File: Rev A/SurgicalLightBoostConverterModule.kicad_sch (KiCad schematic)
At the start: 0 parts

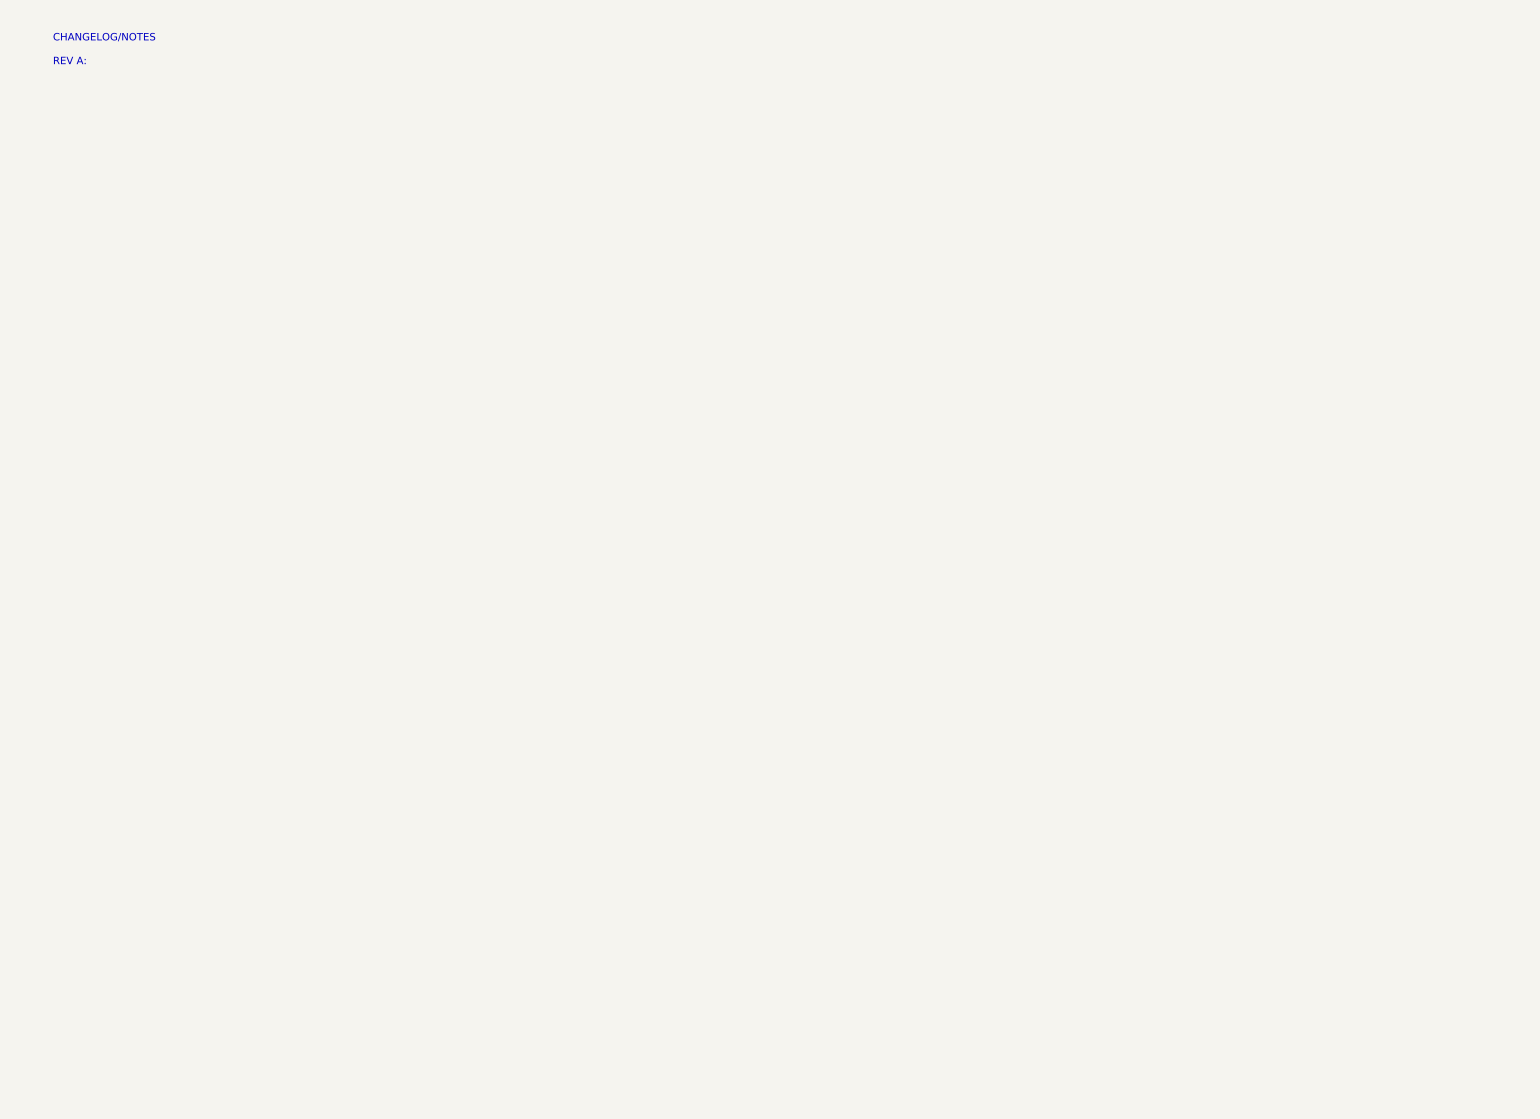
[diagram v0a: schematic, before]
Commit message: Added boost converter.
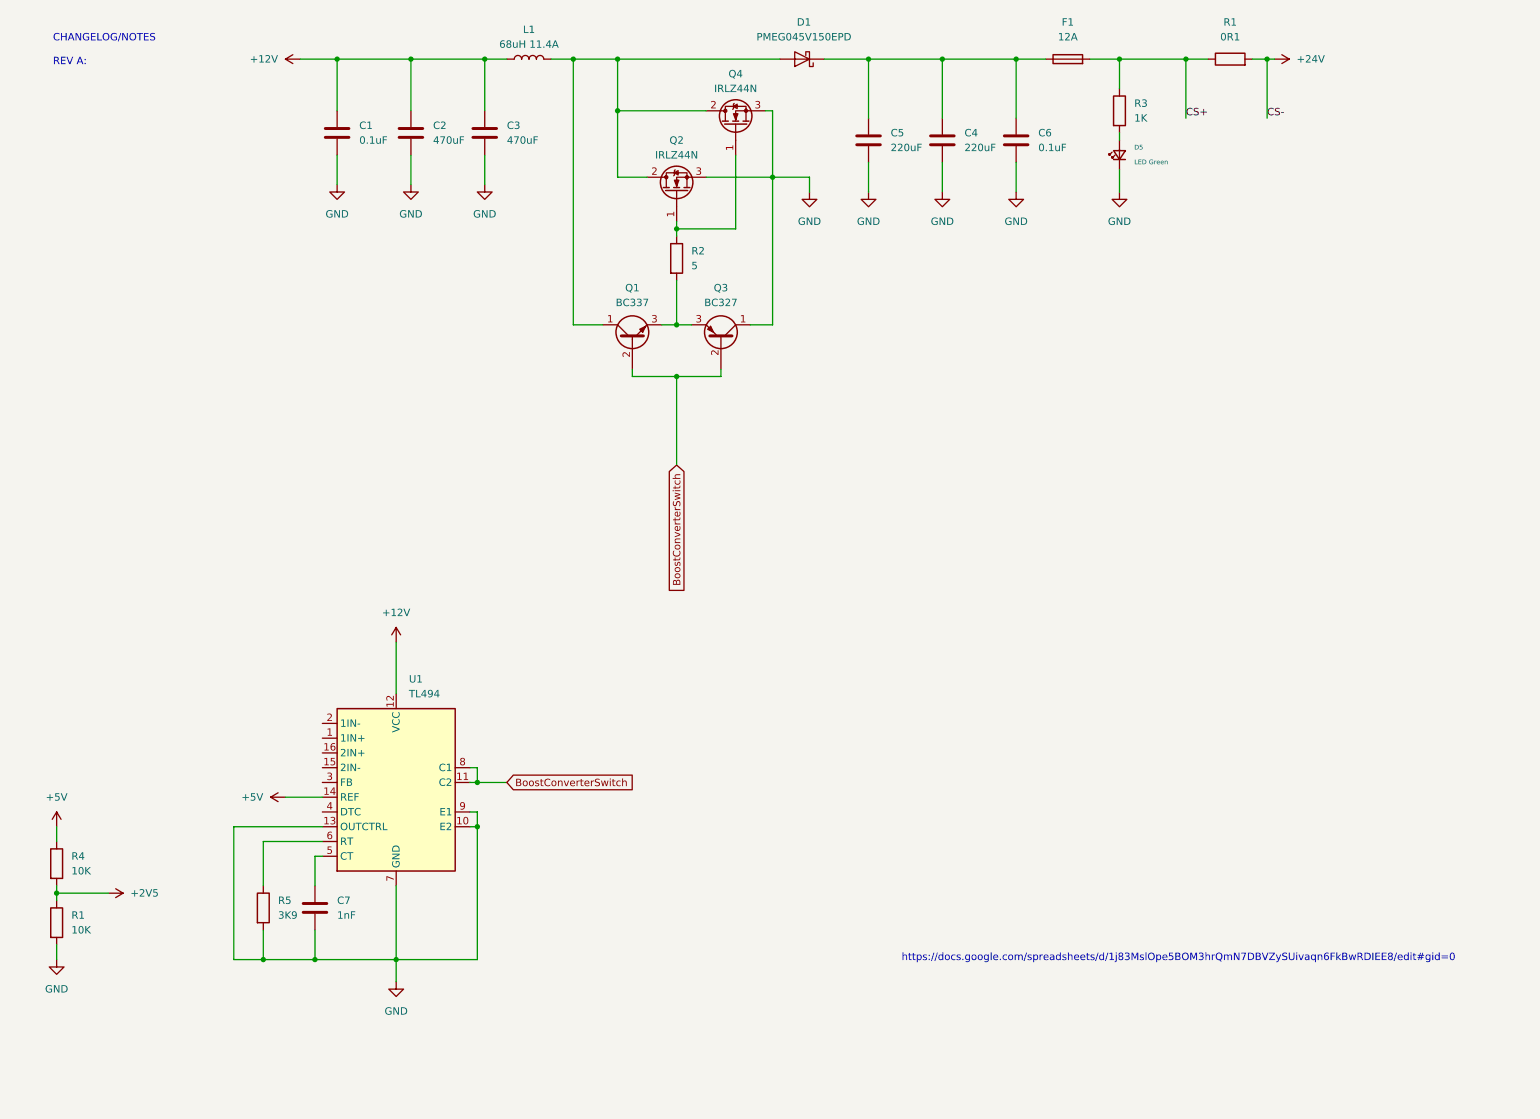
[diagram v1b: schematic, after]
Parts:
- added C1, C6: 0.1uF, Capacitor_SMD:C_0805_2012Metric, symbol Device:C
- added C2, C3: 470uF, symbol Device:C
- added C4, C5: 220uF, symbol Device:C
- added C7: 1nF, Capacitor_SMD:C_0805_2012Metric, symbol Device:C
- added D1: PMEG045V150EPD, Package_TO_SOT_SMD:Nexperia_CFP15_SOT-1289, symbol Diode:PMEG045V150EPD
- added D5: LED Green, LED_SMD:LED_0805_2012Metric, symbol Device:LED_Small
- added F1: 12A, symbol Device:Fuse
- added L1: 68uH 11.4A, symbol Device:L
- added Q1: BC337, Package_TO_SOT_THT:TO-92_Inline, symbol Transistor_BJT:BC337
- added Q2, Q4: IRLZ44N, Package_TO_SOT_THT:TO-220-3_Vertical, symbol Transistor_FET:IRLZ44N
- added Q3: BC327, Package_TO_SOT_THT:TO-92_Inline, symbol Transistor_BJT:BC327
- added R1: 0R1, Resistor_SMD:R_0805_2012Metric, symbol Device:R
- added R1, R4: 10K, Resistor_SMD:R_0805_2012Metric, symbol Device:R
- added R2: 5, Resistor_SMD:R_0805_2012Metric, symbol Device:R
- added R3: 1K, Resistor_SMD:R_0805_2012Metric, symbol Device:R
- added R5: 3K9, Resistor_SMD:R_0805_2012Metric, symbol Device:R
- added U1: TL494, symbol Regulator_Controller:TL494
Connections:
- new net: D1.1 (A), D1.2 (A), L1.2, Q1.1 (C), Q2.2 (D), Q4.2 (D)
- new net: Q1.3 (E), Q3.3 (E), R2.2
- new net: C4.1, C5.1, C6.1, D1.3 (K), F1.1
- new net: R5.1, U1.6 (RT)
- new net: Q2.1 (G), Q4.1 (G), R2.1
- new net: C7.1, U1.5 (CT)
- new net: D5.2 (A), R3.2
- new net +12V: C1.1, C2.1, C3.1, L1.1, U1.12 (VCC)
- new net +24V: R1.2
- new net +2V5: R1.1, R4.2
- new net +5V: R4.1, U1.14 (REF)
- new net BoostConverterSwitch: Q1.2 (B), Q3.2 (B), U1.11 (C2), U1.8 (C1)
- new net CS+: F1.2, R1.1, R3.1
- new net GND: C1.2, C2.2, C3.2, C4.2, C5.2, C6.2, C7.2, D5.1 (K), Q2.3 (S), Q3.1 (C), Q4.3 (S), R1.2, R5.2, U1.10 (E2), U1.13 (OUTCTRL), U1.7 (GND), U1.9 (E1)
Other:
- note added: "https://docs.google.com/spreadsheets/d/1j83MslOpe5BOM3hrQmN7DBVZySUivaqn6FkBwRDIEE8/edit#gid=0"

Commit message: Added feedback and protection circuits.
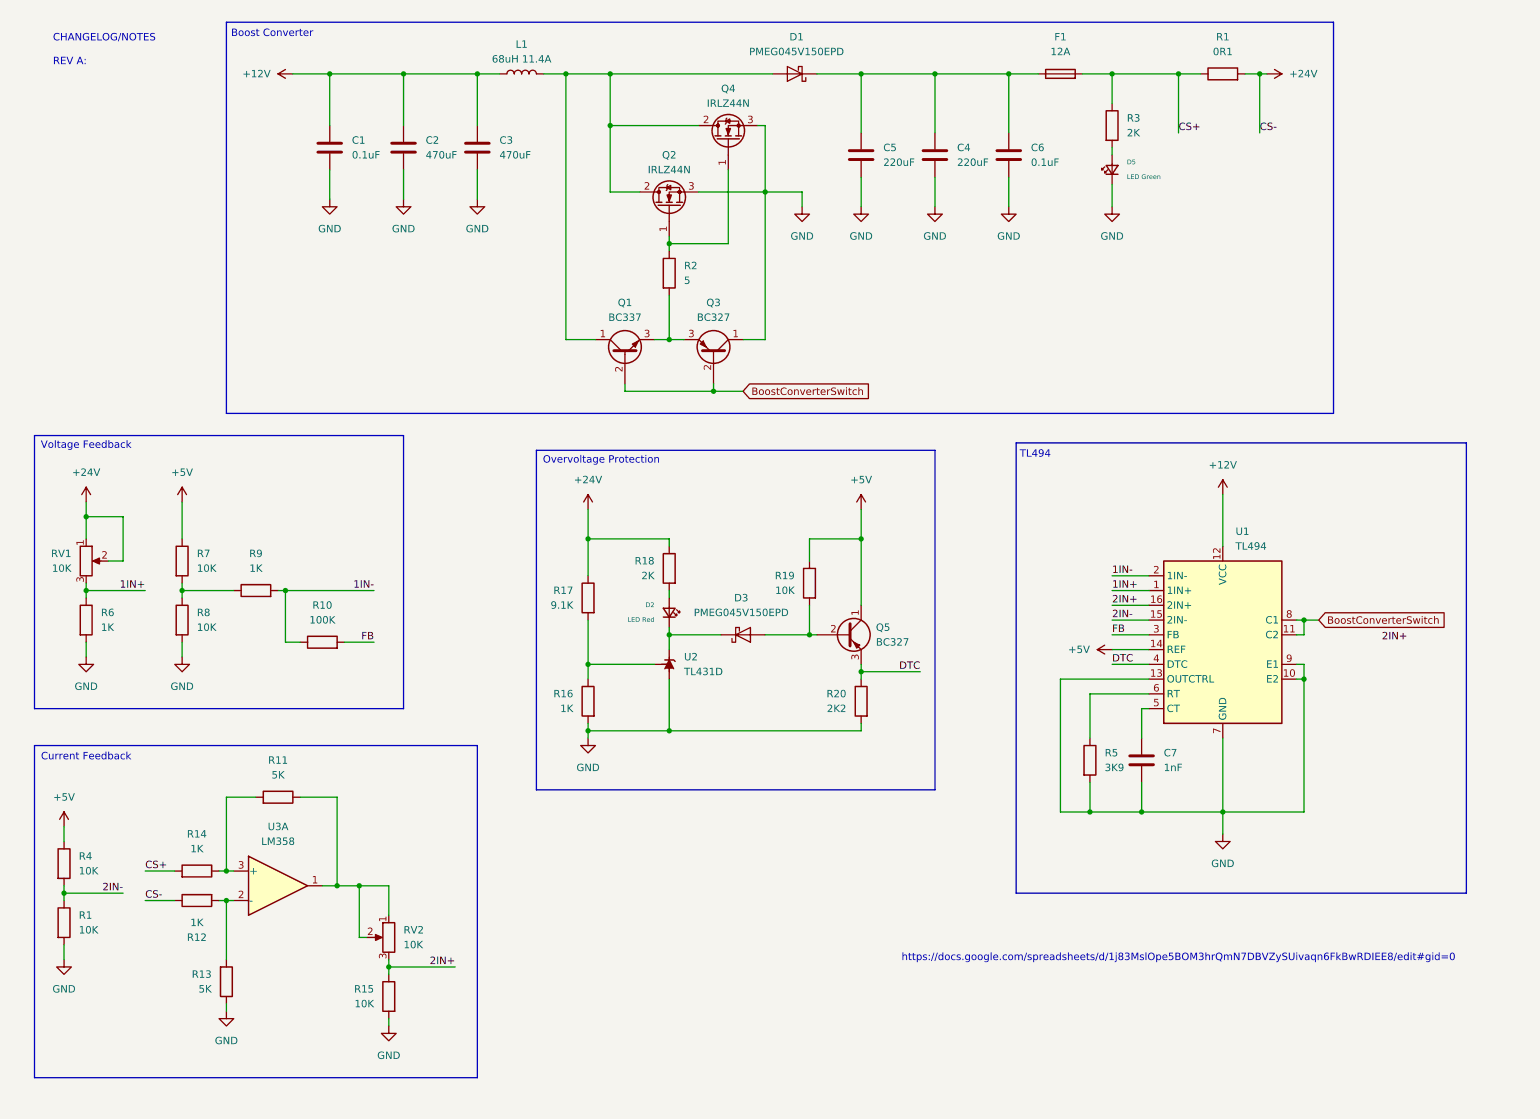
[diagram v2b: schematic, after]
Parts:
- added D2: LED Red, LED_SMD:LED_0805_2012Metric, symbol Device:LED_Small
- added D3: PMEG045V150EPD, Package_TO_SOT_SMD:Nexperia_CFP15_SOT-1289, symbol Diode:PMEG045V150EPD
- added Q5: BC327, Package_TO_SOT_THT:TO-92_Inline, symbol Transistor_BJT:BC327
- added R10: 100K, Resistor_SMD:R_0805_2012Metric, symbol Device:R
- added R11, R13: 5K, Resistor_SMD:R_0805_2012Metric, symbol Device:R
- added R12, R14, R16, R6, R9: 1K, Resistor_SMD:R_0805_2012Metric, symbol Device:R
- added R15, R19, R7, R8: 10K, Resistor_SMD:R_0805_2012Metric, symbol Device:R
- added R17: 9.1K, Resistor_SMD:R_0805_2012Metric, symbol Device:R
- added R18: 2K, Resistor_SMD:R_0805_2012Metric, symbol Device:R
- added R20: 2K2, Resistor_SMD:R_0805_2012Metric, symbol Device:R
- added RV1, RV2: 10K, symbol Device:R_Potentiometer
- added U2: TL431D, Package_SO:SOIC-8_3.9x4.9mm_P1.27mm, symbol Reference_Voltage:TL431D
- added U3: LM358, symbol Amplifier_Operational:LM358
- R3: value 1K -> 2K
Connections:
- net +2V5 is gone; now on net 2IN-: R1.1, R4.2
- net +24V: now also R12.1, R17.1, R18.1, RV1.1, RV1.2
- net +5V: now also Q5.1 (C), R19.1, R7.1
- net CS+: now also R14.2
- net GND: now also R13.1, R15.2, R16.2, R20.2, R6.2, R8.2, U2.2 (A), U2.3 (A), U2.6 (A), U2.7 (A)
- net 1IN+: now reaches U1.1 (1IN+)
- net 1IN+: now also R6.1, RV1.3
- net 2IN-: now reaches U1.15 (2IN-)
- net 2IN+: now reaches U1.16 (2IN+)
- net 2IN+: now also R15.1, RV2.3
- net 1IN-: now reaches U1.2 (1IN-)
- net 1IN-: now also R10.1, R9.2
- net FB: now reaches U1.3 (FB)
- net FB: now also R10.2
- net DTC: now reaches U1.4 (DTC)
- net DTC: now also Q5.3 (E), R20.1
- new net: R11.2, R14.1, U3.3 (+)
- new net: R11.1, RV2.1, RV2.2, U3.1
- new net: R12.2, R13.2, U3.2 (-)
- new net: R16.1, R17.2, U2.8 (REF)
- new net: D3.1 (A), D3.2 (A), Q5.2 (B), R19.2
- new net: D2.2 (A), R18.2
- new net: D2.1 (K), D3.3 (K), U2.1 (K)
- new net: R7.2, R8.1, R9.1
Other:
- note added: "Boost Converter"
- note added: "Current Feedback"
- note added: "Overvoltage Protection"
- note added: "TL494"
- note added: "Voltage Feedback"
- moved on the sheet: C1, C2, C3, C4, C5, C6, C7, D1, D5, F1, L1, Q1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

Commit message: More schematic updates.
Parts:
- added D4: LED Green, LED_SMD:LED_0805_2012Metric, symbol Device:LED_Small
- added H1, H2, H3, H4: M3 Hole, MountingHole:MountingHole_3.2mm_M3_Pad_TopBottom, symbol Mechanical:MountingHole_Pad
- added R21: 1K, Resistor_SMD:R_0805_2012Metric, symbol Device:R
- added TP1: 24V, symbol Connector:TestPoint_Small
- added TP2: 5V, symbol Connector:TestPoint_Small
- added TP3: DTC, symbol Connector:TestPoint_Small
- added TP4: PWM, symbol Connector:TestPoint_Small
- added TP5: 2IN+, symbol Connector:TestPoint_Small
- added TP6: 2IN-, symbol Connector:TestPoint_Small
- added TP7: 1IN+, symbol Connector:TestPoint_Small
- added TP8: 1IN-, symbol Connector:TestPoint_Small
- C2, C3: footprint (none) -> Capacitor_THT:CP_Radial_D12.5mm_P5.00mm
- C4, C5: footprint (none) -> Capacitor_THT:CP_Radial_D10.0mm_P5.00mm
- L1: footprint (none) -> Inductor_THT:L_Radial_D29.8mm_P29.30mm_Murata_1400series
- RV1, RV2: footprint (none) -> Connector_PinHeader_2.54mm:PinHeader_1x03_P2.54mm_Vertical
- U1: footprint (none) -> Package_DIP:DIP-16_W7.62mm
- U3: footprint (none) -> Package_DIP:DIP-8_W7.62mm_Socket
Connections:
- net +12V: now also H4.1, R21.1
- net +24V: now also H3.1, TP1.1
- net +5V: now also TP2.1
- net 1IN+: now also TP7.1
- net 1IN-: now also TP8.1
- net 2IN+: now also TP5.1
- net 2IN-: now also TP6.1
- net BoostConverterSwitch: now also TP4.1
- net DTC: now also TP3.1
- net GND: now also D4.1 (K), H1.1, H2.1
- new net: D4.2 (A), R21.2
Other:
- note added: "Mounting Holes for Power Connections"
- moved on the sheet: C1, C2, C4, C5, C6, C7, D1, D2, D3, D5, F1, L1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

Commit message: PCB? :(
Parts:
- added C10, C7: 1uF, Capacitor_SMD:C_0805_2012Metric, symbol Device:C
- added C11, C8: 0.1uF, Capacitor_SMD:C_0805_2012Metric, symbol Device:C
- added D4: LED Green, LED_SMD:LED_0805_2012Metric, symbol Device:LED_Small
- added R2: 0R1, Resistor_SMD:R_2512_6332Metric, symbol Device:R
- added R6: 330, Resistor_SMD:R_0805_2012Metric, symbol Device:R
- added unit 2 of U3
- added unit 3 of U3
- F1: footprint (none) -> Fuse:Fuse_1206_3216Metric_Pad1.42x1.75mm_HandSolder
- R1: footprint Resistor_SMD:R_0805_2012Metric -> Resistor_SMD:R_2512_6332Metric
- R18: renamed from R11; value 5K -> 10K
- R23: renamed from R13; value 5K -> 10K
- R5: renamed from R2; value 5 -> 10
- TP1: renamed from TP4; footprint (none) -> TestPoint:TestPoint_Pad_D2.0mm
- TP2: renamed from TP1; footprint (none) -> TestPoint:TestPoint_Pad_D2.0mm
- TP3: renamed from TP2; footprint (none) -> TestPoint:TestPoint_Pad_D2.0mm
- TP4: renamed from TP8; footprint (none) -> TestPoint:TestPoint_Pad_D2.0mm
- TP5: renamed from TP7; footprint (none) -> TestPoint:TestPoint_Pad_D2.0mm
- TP6: renamed from TP3; footprint (none) -> TestPoint:TestPoint_Pad_D2.0mm
- TP7: renamed from TP6; footprint (none) -> TestPoint:TestPoint_Pad_D2.0mm
- TP8: renamed from TP5; footprint (none) -> TestPoint:TestPoint_Pad_D2.0mm
- renumbered C5 to C4, C4 to C5, C7 to C9, D5 to D2, D4 to D3, D2 to D5, D3 to D6, Q4 to Q1, Q1 to Q3, Q3 to Q4, R17 to R10, R9 to R11, R6 to R12, R8 to R13, R10 to R14, R16 to R15, R20 to R16, R5 to R17, R4 to R19, R14 to R20, R1 to R21, R12 to R22, R15 to R24, R21 to R4, R18 to R7, R7 to R8, R19 to R9
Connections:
- net +12V: now also C10.1, C11.1, C7.1, C8.1, U3.8 (V+)
- net +24V: now also R2.2
- net +5V: now also R6.1
- net CS+: now also R2.1
- net GND: now also C10.2, C11.2, C7.2, C8.2, D4.1 (K), U3.4 (V-), U3.5 (+), U3.6 (-), U3.7
- new net: D4.2 (A), R6.2
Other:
- moved on the sheet: C1, C2, C3, C4, C5, C6, C9, D1, D2, D3, D5, D6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

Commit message: added michael's changes
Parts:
- removed Q1, Q2: IRLZ44N, Package_TO_SOT_THT:TO-220-3_Vertical, symbol Transistor_FET:IRLZ44N
- removed Q4: BC327, Package_TO_SOT_THT:TO-92_Inline, symbol Transistor_BJT:BC327
- removed R2: 0R1, Resistor_SMD:R_2512_6332Metric, symbol Device:R
- added C10, C7, C8, C9: 0.1uF, Capacitor_SMD:C_0805_2012Metric, symbol Device:C
- added D2, D5, D6: PMEG045V150EPD, Package_TO_SOT_SMD:Nexperia_CFP15_SOT-1289, symbol Diode:PMEG045V150EPD
- added J1: 2x7 P2.54mm, Connector_PinHeader_2.54mm:PinHeader_2x07_P2.54mm_Vertical, symbol Connector_Generic:Conn_02x07_Odd_Even
- added Q1, Q2: BC337, Package_TO_SOT_THT:TO-92_Inline, symbol Transistor_BJT:BC337
- added Q4, Q5, Q6: IRLZ44N, Package_TO_SOT_THT:TO-220-3_Vertical, symbol Transistor_FET:IRLZ44N
- added Q7, Q8, Q9: BC327, Package_TO_SOT_THT:TO-92_Inline, symbol Transistor_BJT:BC327
- added R4, R6: 10, Resistor_SMD:R_0805_2012Metric, symbol Device:R
- added TP11: CS+, TestPoint:TestPoint_Loop_D2.54mm_Drill1.5mm_Beaded, symbol Connector:TestPoint_Small
- added TP13: CS-, TestPoint:TestPoint_Loop_D2.54mm_Drill1.5mm_Beaded, symbol Connector:TestPoint_Small
- added TP2: LMount2, TestPoint:TestPoint_Loop_D2.54mm_Drill1.5mm_Beaded, symbol Connector:TestPoint_Small
- added TP3: LMount4, TestPoint:TestPoint_Loop_D2.54mm_Drill1.5mm_Beaded, symbol Connector:TestPoint_Small
- added TP4: LMount3, TestPoint:TestPoint_Loop_D2.54mm_Drill1.5mm_Beaded, symbol Connector:TestPoint_Small
- added TP9: PWM, TestPoint:TestPoint_Loop_D2.54mm_Drill1.5mm_Beaded, symbol Connector:TestPoint_Small
- F1: footprint Fuse:Fuse_1206_3216Metric_Pad1.42x1.75mm_HandSolder -> Fuse:Fuseholder_Clip-6.3x32mm_Littelfuse_102071_Inline_P34.70x7.60mm_D2.00mm_Horizontal
- R1: value 0R1 -> 5mR
- R19: renamed from R18; value 10K -> 100K
- R24: renamed from R23; value 10K -> 100K
- TP1: value PWM -> LMount1; footprint TestPoint:TestPoint_Pad_D2.0mm -> TestPoint:TestPoint_Loop_D2.54mm_Drill1.5mm_Beaded
- TP10: renamed from TP6; footprint TestPoint:TestPoint_Pad_D2.0mm -> TestPoint:TestPoint_Loop_D2.54mm_Drill1.5mm_Beaded
- TP12: renamed from TP7; footprint TestPoint:TestPoint_Pad_D2.0mm -> TestPoint:TestPoint_Loop_D2.54mm_Drill1.5mm_Beaded
- TP14: renamed from TP8; footprint TestPoint:TestPoint_Pad_D2.0mm -> TestPoint:TestPoint_Loop_D2.54mm_Drill1.5mm_Beaded
- TP5: renamed from TP2; footprint TestPoint:TestPoint_Pad_D2.0mm -> TestPoint:TestPoint_Loop_D2.54mm_Drill1.5mm_Beaded
- TP6: renamed from TP3; footprint TestPoint:TestPoint_Pad_D2.0mm -> TestPoint:TestPoint_Loop_D2.54mm_Drill1.5mm_Beaded
- TP7: renamed from TP4; footprint TestPoint:TestPoint_Pad_D2.0mm -> TestPoint:TestPoint_Loop_D2.54mm_Drill1.5mm_Beaded
- TP8: renamed from TP5; footprint TestPoint:TestPoint_Pad_D2.0mm -> TestPoint:TestPoint_Loop_D2.54mm_Drill1.5mm_Beaded
- U2: footprint Package_SO:SOIC-8_3.9x4.9mm_P1.27mm -> Package_DIP:DIP-8_W7.62mm_Socket
- renumbered C2 to C1, C7 to C11, C8 to C12, C9 to C13, C10 to C14, C11 to C15, C3 to C2, C4 to C3, C5 to C4, C1 to C5, D2 to D3, D3 to D4, D4 to D7, D5 to D8, D6 to D9, H3 to H1, H4 to H2, H1 to H3, H2 to H4, Q5 to Q10, R9 to R10, R10 to R11, R11 to R12, R12 to R13, R13 to R14, R14 to R15, R15 to R16, R16 to R17, R17 to R18, R3 to R2, R19 to R20, R20 to R21, R21 to R22, R22 to R23, R24 to R25, R4 to R3, R6 to R7, R7 to R8, R8 to R9
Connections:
- net +12V: now also C6.1, C7.1
- net +24V: now also F1.2; no longer R1.2, R11.1, R23.1, R8.1, RV1.1, RV1.2, TP5.1
- net 1IN-: now also J1.4 (Pin_4)
- net 2IN-: now also J1.8 (Pin_8)
- net BoostConverterSwitch: now also Q1.2 (B), Q2.2 (B), Q7.2 (B), Q8.2 (B), Q9.2 (B), TP9.1; no longer TP1.1
- net CS+: now also C3.1, C4.1, D1.3 (K), R11.1, R8.1, RV1.1, RV1.2, TP5.1, C10.1, C8.1, C9.1, D2.3 (K), D5.3 (K), D6.3 (K), TP11.1; no longer F1.2, R2.1
- net DTC: now also J1.12 (Pin_12)
- net GND: now also C10.2, C7.2, C8.2, C9.2, J1.14 (Pin_14), Q4.3 (S), Q5.3 (S), Q6.3 (S), Q7.1 (C), Q8.1 (C), Q9.1 (C)
- net VSwitch: now reaches D1.1 (A), D1.2 (A), L1.2, Q3.1 (C)
- net VSwitch: now also D2.1 (A), D2.2 (A), D5.1 (A), D5.2 (A), D6.1 (A), D6.2 (A), Q1.1 (C), Q2.1 (C), Q4.2 (D), Q5.2 (D), Q6.2 (D)
- net at Q3.3 (E): now also Q9.3 (E), R6.1; no longer R5.2
- net at R5.1: now also Q2.3 (E), Q8.3 (E)
- new net: Q1.3 (E), Q7.3 (E), R4.1
- new net: Q4.1 (G), R4.2
- new net: Q6.1 (G), R6.2
- new net: Q5.1 (G), R5.2
- new net CS-: F1.1, R1.2, R2.1, R23.1, TP13.1
- no-connect marks 0 -> 14
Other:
- note added: "Header Connections"
- note added: "Mounting/Power Holes"
- note removed: "Mounting Holes for Power Connections"
- moved on the sheet: C1, C11, C12, C13, C2, C3, C4, C5, D1, D3, D4, H1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
